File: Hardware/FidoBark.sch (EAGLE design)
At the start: 30 parts, among them IC1 STM32F405RGT, J4 MICRO-SDCARD-CONNECTOR-330006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, Y1_8MHZ 631-1100-ND, Y2_32.768KHZ 32.768KHz

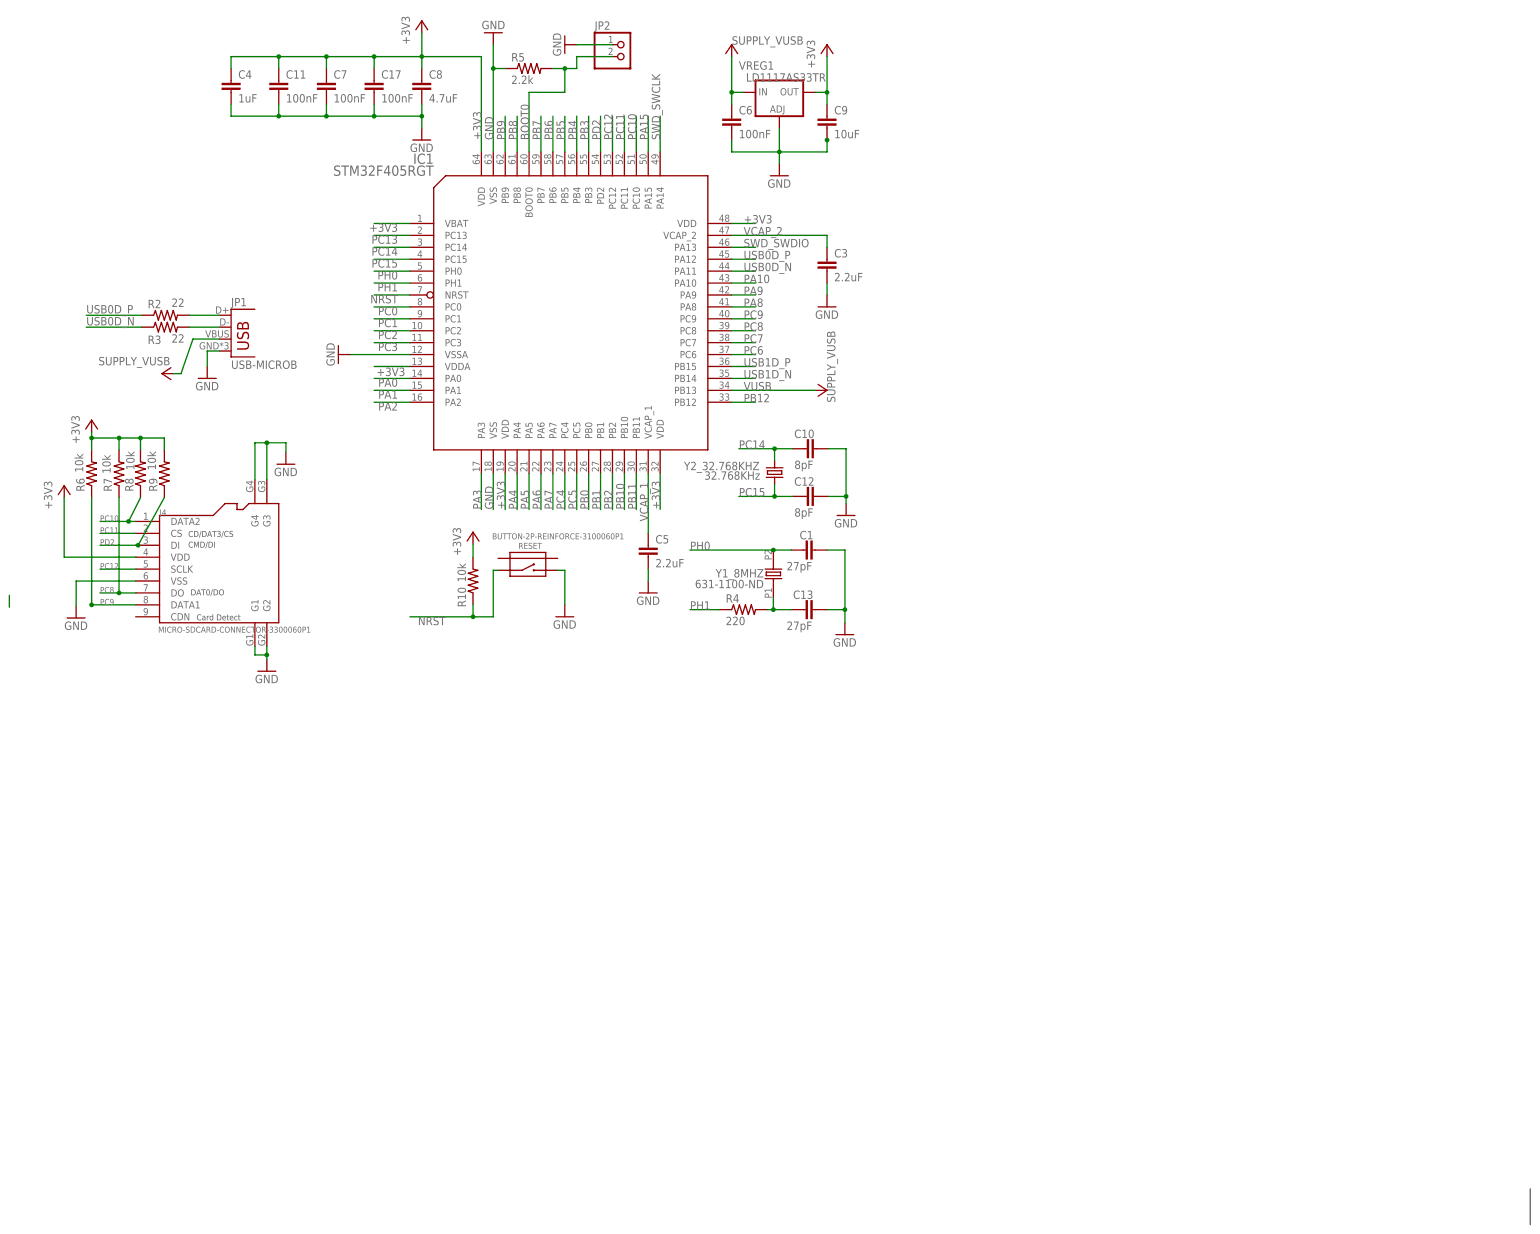
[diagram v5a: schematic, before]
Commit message: teensy and SD card
trying a faster route
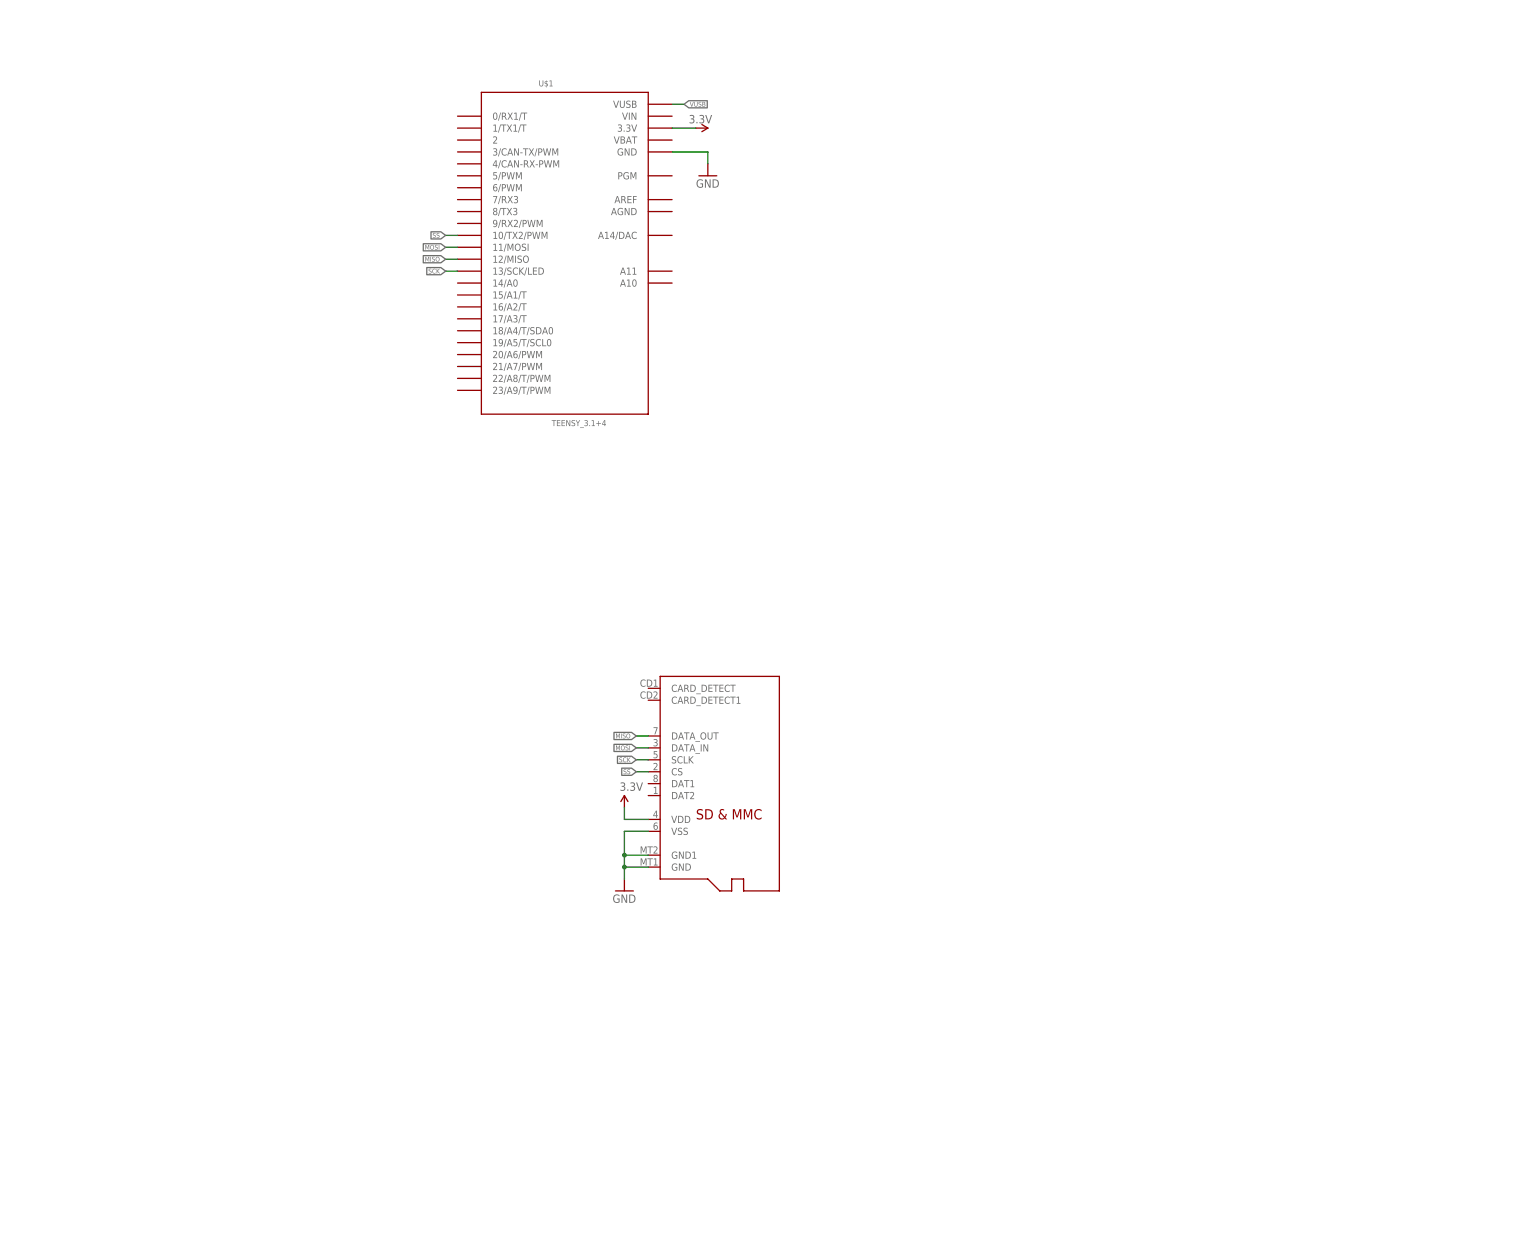
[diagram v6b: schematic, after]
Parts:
- removed C1, C13: 27pF, rcl:C-EUC0603
- removed C10, C12: 8pF, rcl:C-EUC0603
- removed C11, C17, C6, C7: 100nF, rcl:C-EUC0603
- removed C3, C5: 2.2uF, rcl:C-EUC0603
- removed C4: 1uF, rcl:C-EUC0603
- removed C8: 4.7uF, rcl:C-EUC0603
- removed C9: 10uF, rcl:C-EUC0603
- removed IC1: STM32F405RGT, 0ben:STM32F405RGT
- removed J4: MICRO-SDCARD-CONNECTOR-3300060P1, OPL:MICRO-SDCARD-CONNECTOR-3300060P1
- removed JP1: USB-MICROB, SparkFun-Connectors:USB-MICROB
- removed JP2: (no value), pinhead:PINHD-1X2
- removed R10, R6, R7, R8, R9: 10k, rcl:R-US_R0603
- removed R2, R3: 22, rcl:R-US_R0603
- removed R4: 220, rcl:R-US_R0603
- removed R5: 2.2k, rcl:R-US_R0603
- removed RESET: BUTTON-2P-REINFORCE-3100060P1, OPL:BUTTON-2P-REINFORCE-3100060P1
- removed VREG1: LD1117AS33TR, v-reg:LD117AS33TR
- removed Y1_8MHZ: 631-1100-ND, dp_devices:OSC-XTAL-HC-49U-PTH
- removed Y2_32.768KHZ: 32.768KHz, SparkFun:CRYSTALTC38H
- added U$1: TEENSY_3.1+4, Teensy_3_Series_Board_v1.0:TEENSY_3.1+4
- added U$2: MICROSD, adafruit:MICROSD
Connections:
- removed net +3V3: C11.1, C17.1, C4.1, C7.1, C8.1, C9.1, IC1.VBAT, IC1.VDD@19, IC1.VDD@32, IC1.VDD@48, IC1.VDD@64, IC1.VDDA, J4.VDD, R10.2, R6.2, R7.2, R8.2, R9.2, VREG1.OUT
- removed net BOOT0: IC1.BOOT0, JP2.2, R5.2
- removed net N$1: C13.1, R4.2, Y1_8MHZ.1
- removed net NRST: IC1.NRST, R10.1, RESET.1
- removed net PA0: IC1.PA0
- removed net PA1: IC1.PA1
- removed net PA10: IC1.PA10
- removed net PA15: IC1.PA15
- removed net PA2: IC1.PA2
- removed net PA3: IC1.PA3
- removed net PA4: IC1.PA4
- removed net PA5: IC1.PA5
- removed net PA6: IC1.PA6
- removed net PA7: IC1.PA7
- removed net PA8: IC1.PA8
- removed net PA9: IC1.PA9
- removed net PB0: IC1.PB0
- removed net PB1: IC1.PB1
- removed net PB10: IC1.PB10
- removed net PB11: IC1.PB11
- removed net PB12: IC1.PB12
- removed net PB2: IC1.PB2
- removed net PB3: IC1.PB3
- removed net PB4: IC1.PB4
- removed net PB5: IC1.PB5
- removed net PB6: IC1.PB6
- removed net PB7: IC1.PB7
- removed net PB8: IC1.PB8
- removed net PB9: IC1.PB9
- removed net PC0: IC1.PC0
- removed net PC1: IC1.PC1
- removed net PC10: IC1.PC10, J4.DATA2, R8.1
- removed net PC11: IC1.PC11, J4.CS
- removed net PC12: IC1.PC12, J4.SCLK
- removed net PC13: IC1.PC13
- removed net PC14: C10.1, IC1.PC14, Y2_32.768KHZ.2
- removed net PC15: C12.1, IC1.PC15, Y2_32.768KHZ.1
- removed net PC2: IC1.PC2
- removed net PC3: IC1.PC3
- removed net PC4: IC1.PC4
- removed net PC5: IC1.PC5
- removed net PC6: IC1.PC6
- removed net PC7: IC1.PC7
- removed net PC8: IC1.PC8, J4.DO, R7.1
- removed net PC9: IC1.PC9, J4.DATA1, R6.1
- removed net PD2: IC1.PD2, J4.DI, R9.1
- removed net PH0: C1.1, IC1.PH0, Y1_8MHZ.2
- removed net PH1: IC1.PH1, R4.1
- removed net SWD_SWCLK: IC1.PA14
- removed net SWD_SWDIO: IC1.PA13
- removed net USB0D_N: IC1.PA11, R3.1
- removed net USB0D_P: IC1.PA12, R2.1
- removed net USB0_D+: JP1.D+, R2.2
- removed net USB0_D-: JP1.D-, R3.2
- removed net USB1D_N: IC1.PB14
- removed net USB1D_P: IC1.PB15
- removed net VCAP_1: C5.1, IC1.VCAP_1
- removed net VCAP_2: C3.1, IC1.VCAP_2
- new net 3.3V: U$1.3.3V, U$2.VDD
- new net MISO: U$1.12/MISO, U$2.DATA_OUT
- new net MOSI: U$1.11/MOSI, U$2.DATA_IN
- new net SCK: U$1.13/SCK/LED, U$2.SCLK
- new net SS: U$1.10/TX2/PWM, U$2.CS
- net GND: now also U$1.GND, U$2.GND, U$2.GND1, U$2.VSS; no longer C1.2, C10.2, C11.2, C12.2, C13.2, C17.2, C3.2, C4.2, C5.2, C6.2, C7.2, C8.2, C9.2, IC1.VSS@18, IC1.VSS@63, IC1.VSSA, J4.G1, J4.G2, J4.G3, J4.G4, J4.VSS, JP1.GND, JP2.1, R5.1, RESET.2, VREG1.ADJ
- net VUSB: now also U$1.VUSB; no longer C6.1, IC1.PB13, JP1.VBUS, VREG1.IN
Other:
- note removed: "CD/DAT3/CS"
- note removed: "CMD/DI"
- note removed: "Card Detect"
- note removed: "DAT0/DO"

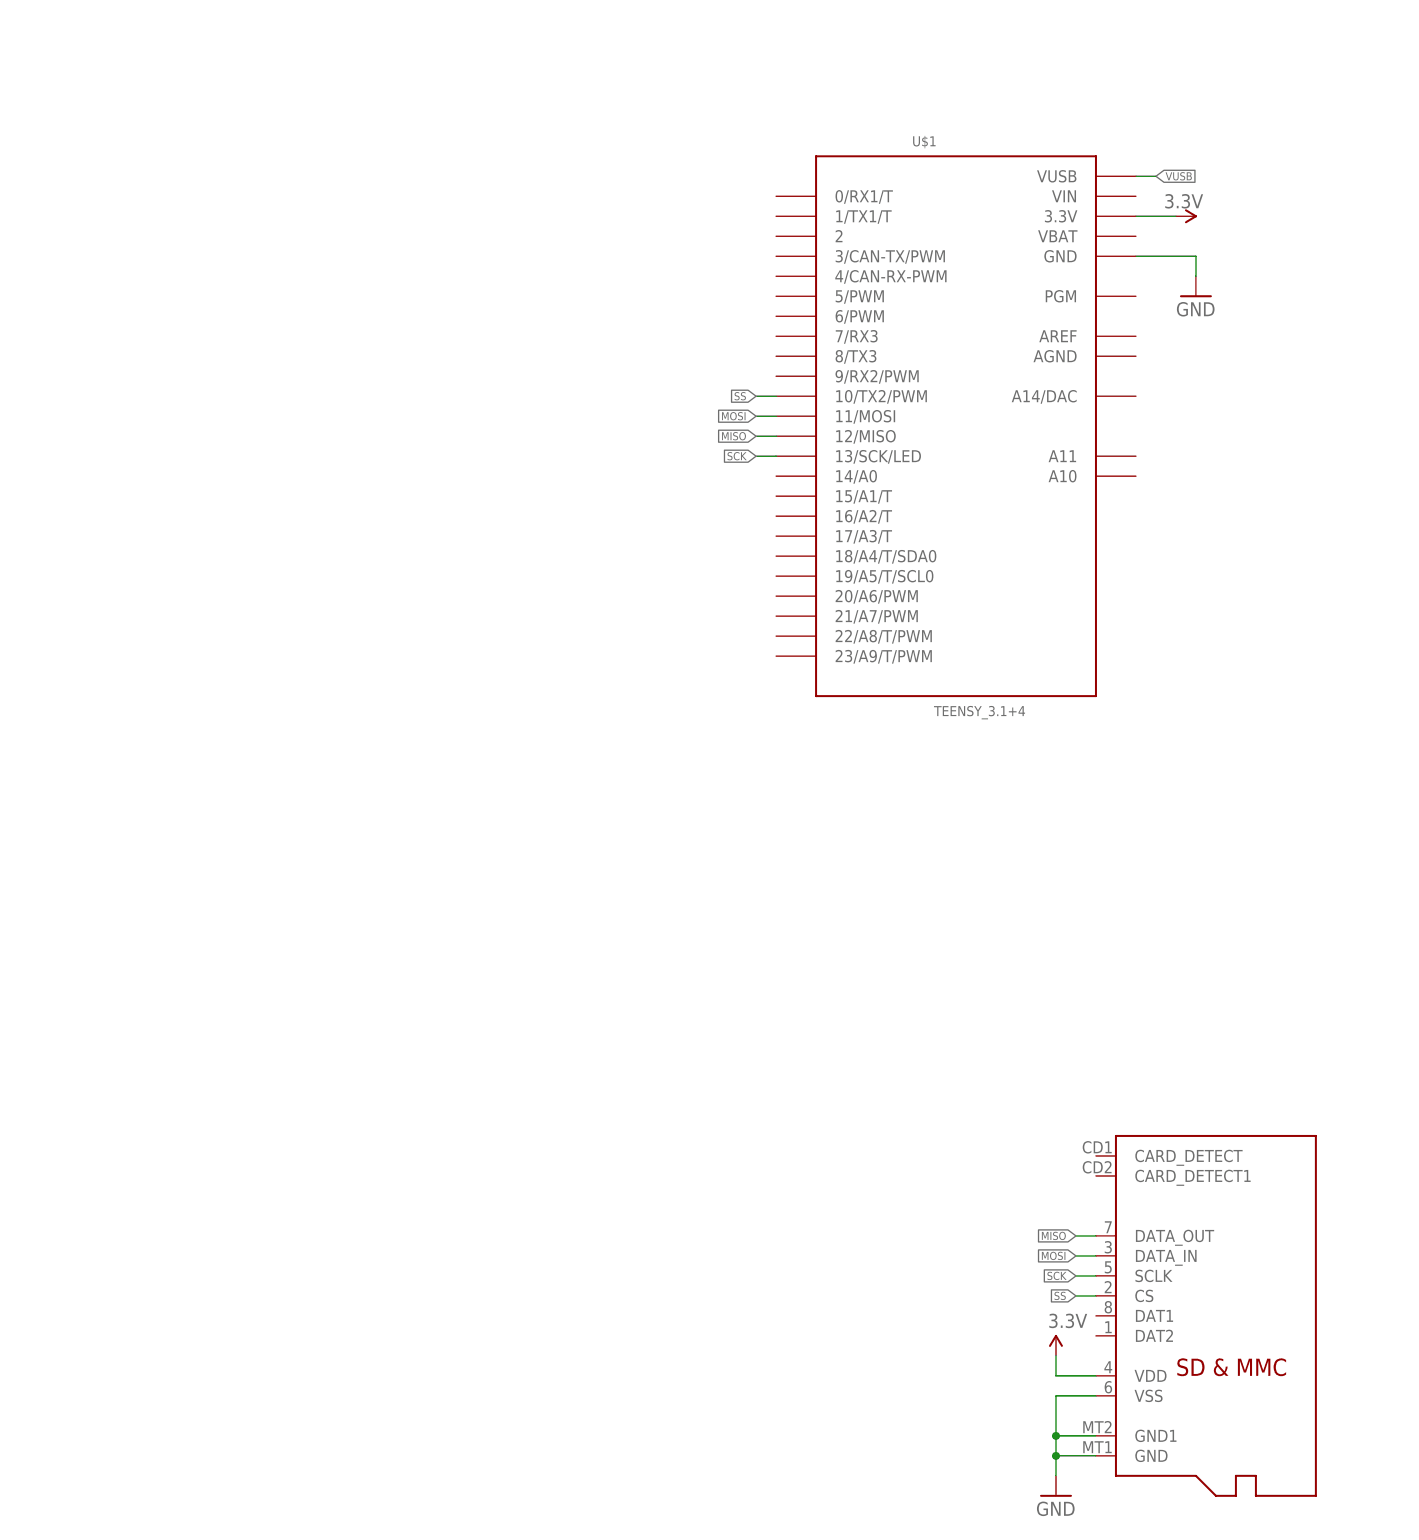
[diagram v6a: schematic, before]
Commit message: motor control, LED, IMU, and piezo
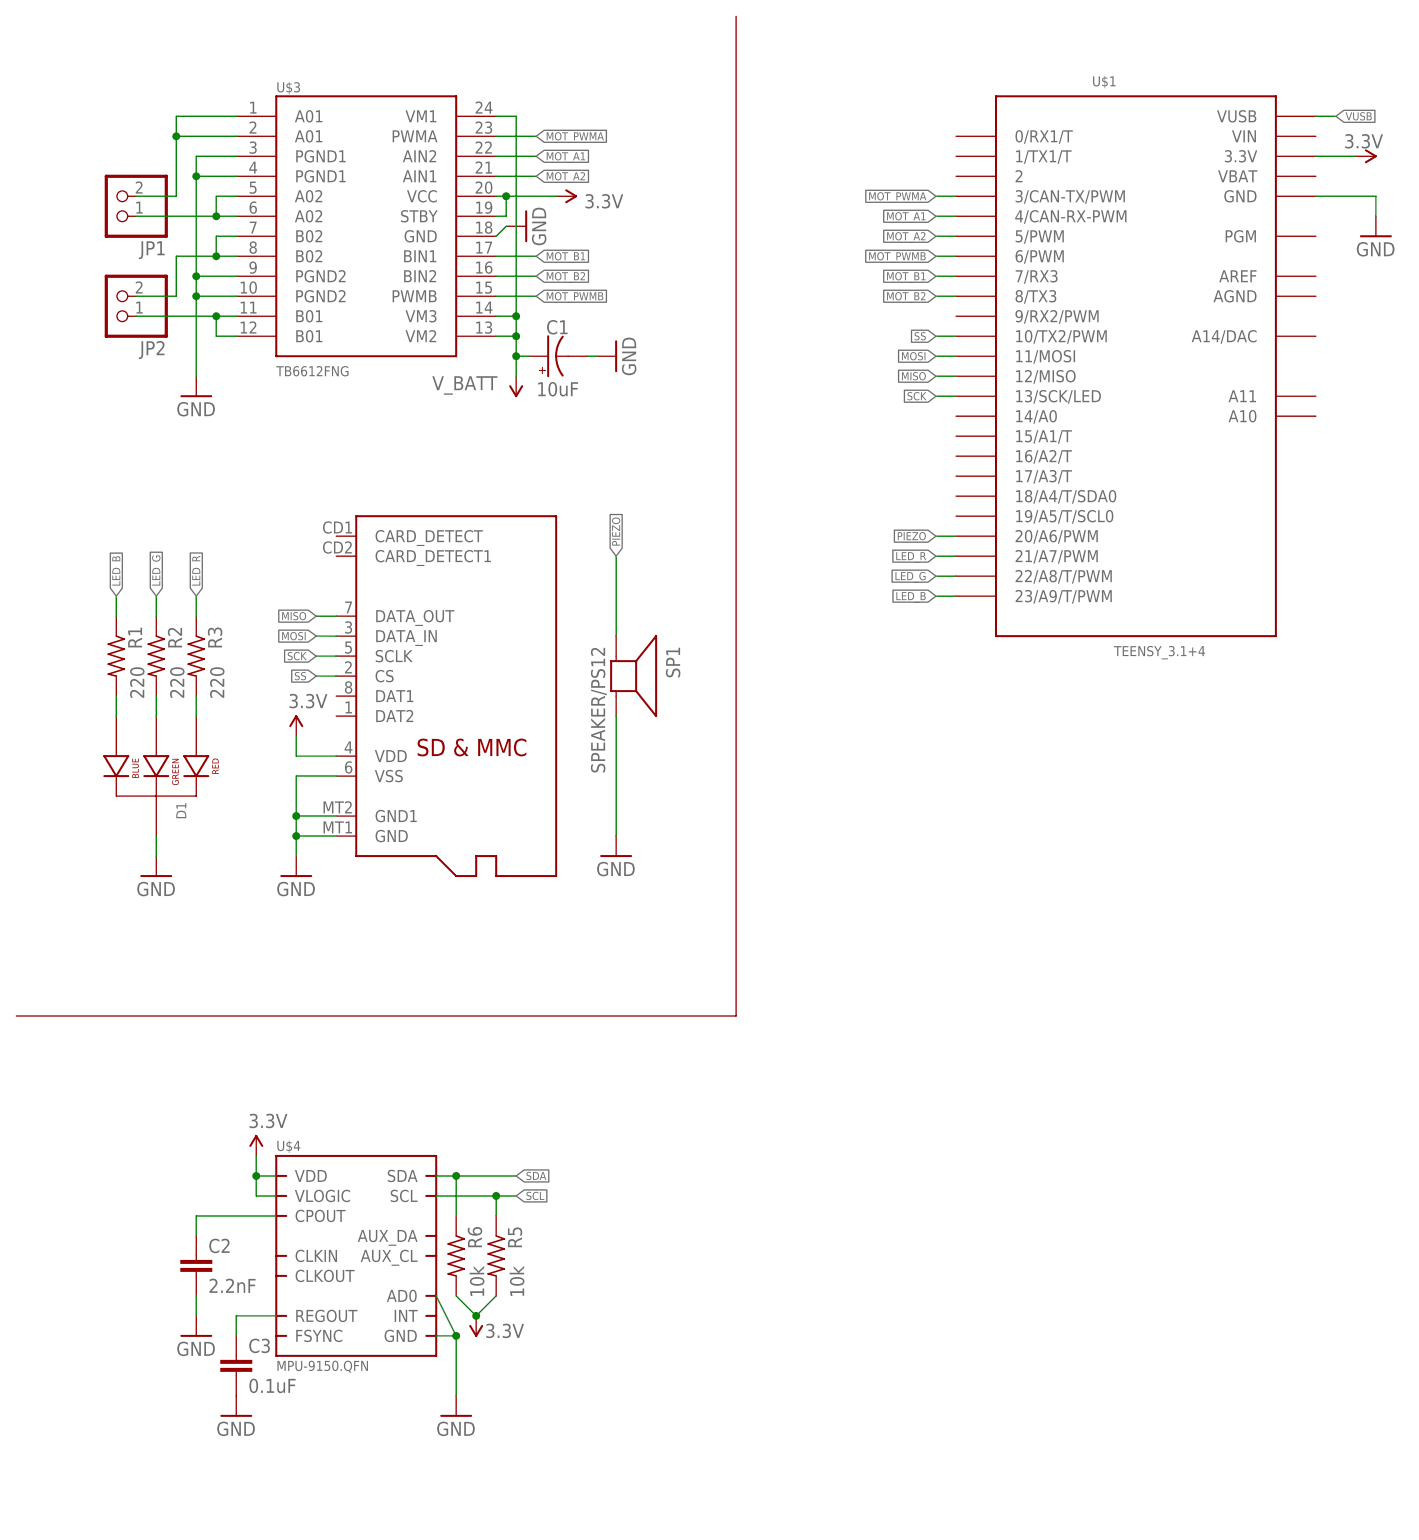
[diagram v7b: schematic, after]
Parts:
- added C1: 10uF, SparkFun-Capacitors:CAP_POL1206
- added C2: 2.2nF, rcl:C-EUC0603
- added C3: 0.1uF, rcl:C-EUC0603
- added D1: LED-RGB-CC-THRUCLEAR, SparkFun-LED:LED-RGB-CC-THRUCLEAR
- added JP1, JP2: (no value), pinhead:PINHD-1X2
- added R1, R2, R3: 220, rcl:R-US_R0603
- added R5, R6: 10k, rcl:R-US_R0603
- added SP1: SPEAKER/PS12, adafruit:SPEAKER/PS12
- added U$3: TB6612FNG, SparkFun-PowerIC:TB6612FNG
- added U$4: MPU-9150.QFN, invensense:MPU-9150.QFN
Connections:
- new net LED_B: R1.1, U$1.23/A9/T/PWM
- new net LED_G: R2.1, U$1.22/A8/T/PWM
- new net LED_R: R3.1, U$1.21/A7/PWM
- new net MOT_A1: U$1.4/CAN-RX-PWM, U$3.AIN2
- new net MOT_A2: U$1.5/PWM, U$3.AIN1
- new net MOT_B1: U$1.7/RX3, U$3.BIN1
- new net MOT_B2: U$1.8/TX3, U$3.BIN2
- new net MOT_PWMA: U$1.3/CAN-TX/PWM, U$3.PWMA
- new net MOT_PWMB: U$1.6/PWM, U$3.PWMB
- new net N$1: JP1.2, U$3.A01@1, U$3.A01@2
- new net N$2: D1.BLUE_CATHODE, R1.2
- new net N$3: JP1.1, U$3.A02@5, U$3.A02@6
- new net N$4: JP2.2, U$3.B02@7, U$3.B02@8
- new net N$5: JP2.1, U$3.B01@11, U$3.B01@12
- new net N$6: D1.GREEN_CATHODE, R2.2
- new net N$7: D1.RED_CATHODE, R3.2
- new net N$8: C3.1, U$4.REGOUT
- new net N$9: C2.1, U$4.CPOUT
- new net PIEZO: SP1.+, U$1.20/A6/PWM
- new net SCL: R5.1, U$4.SCL
- new net SDA: R6.1, U$4.SDA
- new net V_BATT: C1.+, U$3.VM1, U$3.VM2, U$3.VM3
- net 3.3V: now also R5.2, R6.2, U$3.STBY, U$3.VCC, U$4.VDD, U$4.VLOGIC
- net GND: now also C1.-, C2.2, C3.2, D1.CATHODE, SP1.-, U$3.GND, U$3.PGND1@3, U$3.PGND1@4, U$3.PGND2@10, U$3.PGND2@9, U$4.AD0, U$4.GND
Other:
- moved on the sheet: U$1
